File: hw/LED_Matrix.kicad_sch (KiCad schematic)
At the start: 0 parts

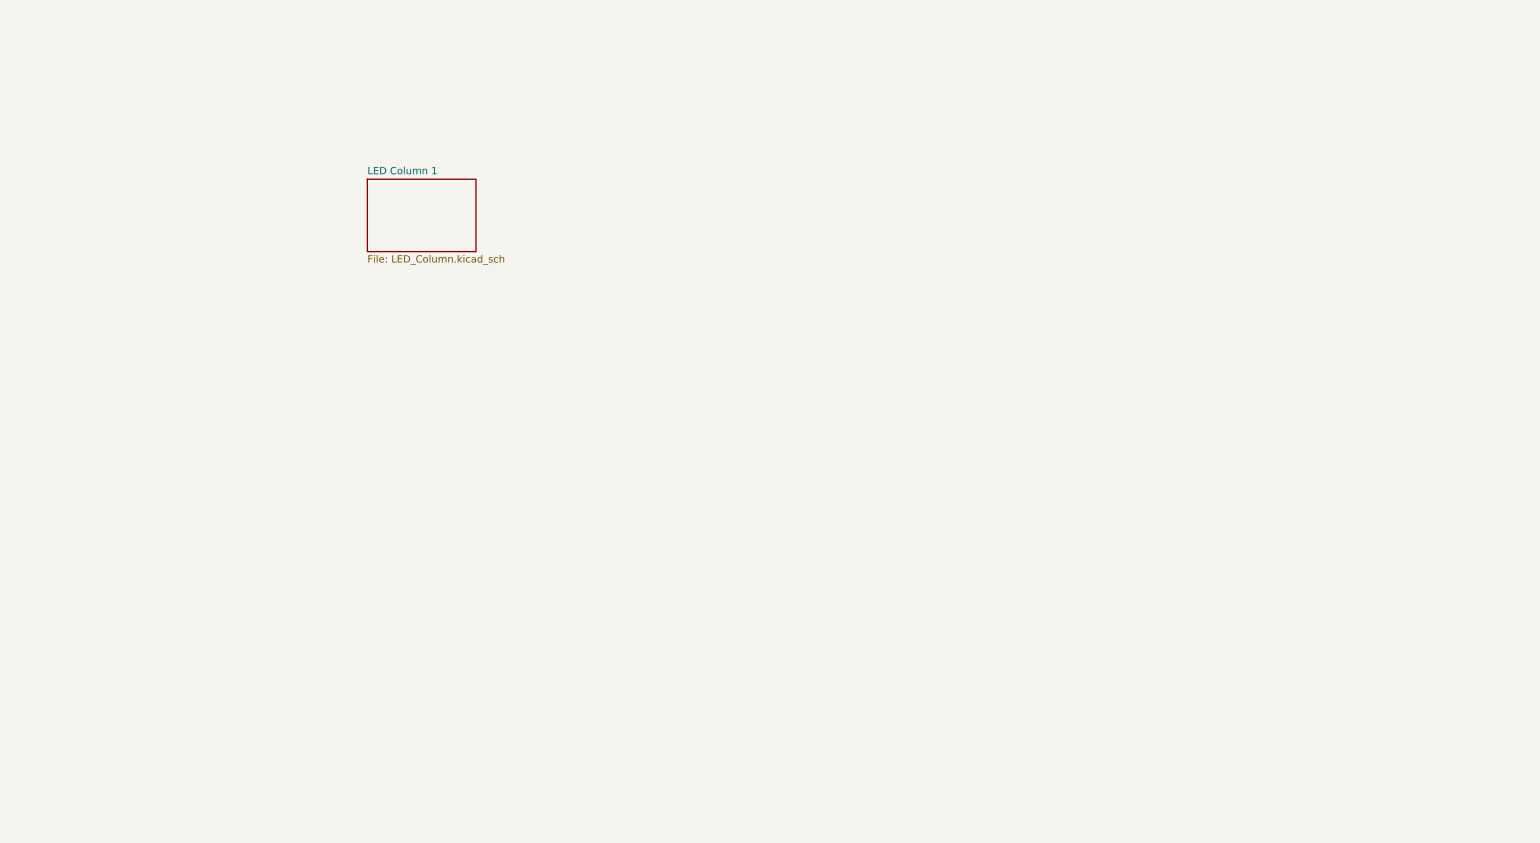
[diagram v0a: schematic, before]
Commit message: added LED Matrix sch
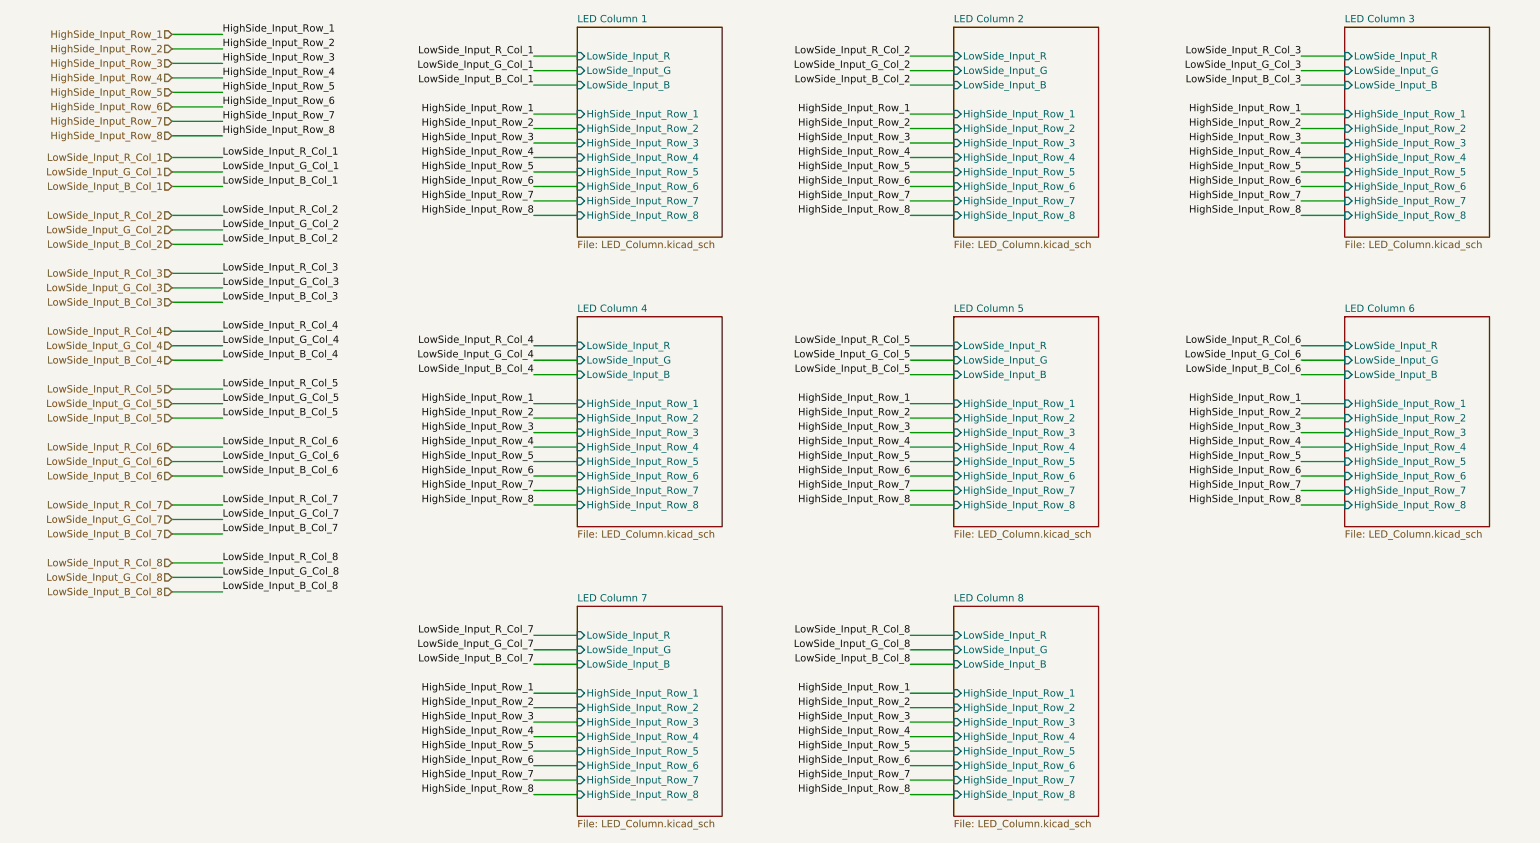
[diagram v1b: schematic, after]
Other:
- added sheet LED Column 2 (LED_Column.kicad_sch)
- added sheet LED Column 3 (LED_Column.kicad_sch)
- added sheet LED Column 4 (LED_Column.kicad_sch)
- added sheet LED Column 5 (LED_Column.kicad_sch)
- added sheet LED Column 6 (LED_Column.kicad_sch)
- added sheet LED Column 7 (LED_Column.kicad_sch)
- added sheet LED Column 8 (LED_Column.kicad_sch)
- sheet LED Column 1 ports: added HighSide_Input_Row_1, HighSide_Input_Row_2, HighSide_Input_Row_3, HighSide_Input_Row_4, HighSide_Input_Row_5, HighSide_Input_Row_6, HighSide_Input_Row_7, HighSide_Input_Row_8, LowSide_Input_B, LowSide_Input_G, LowSide_Input_R; removed none

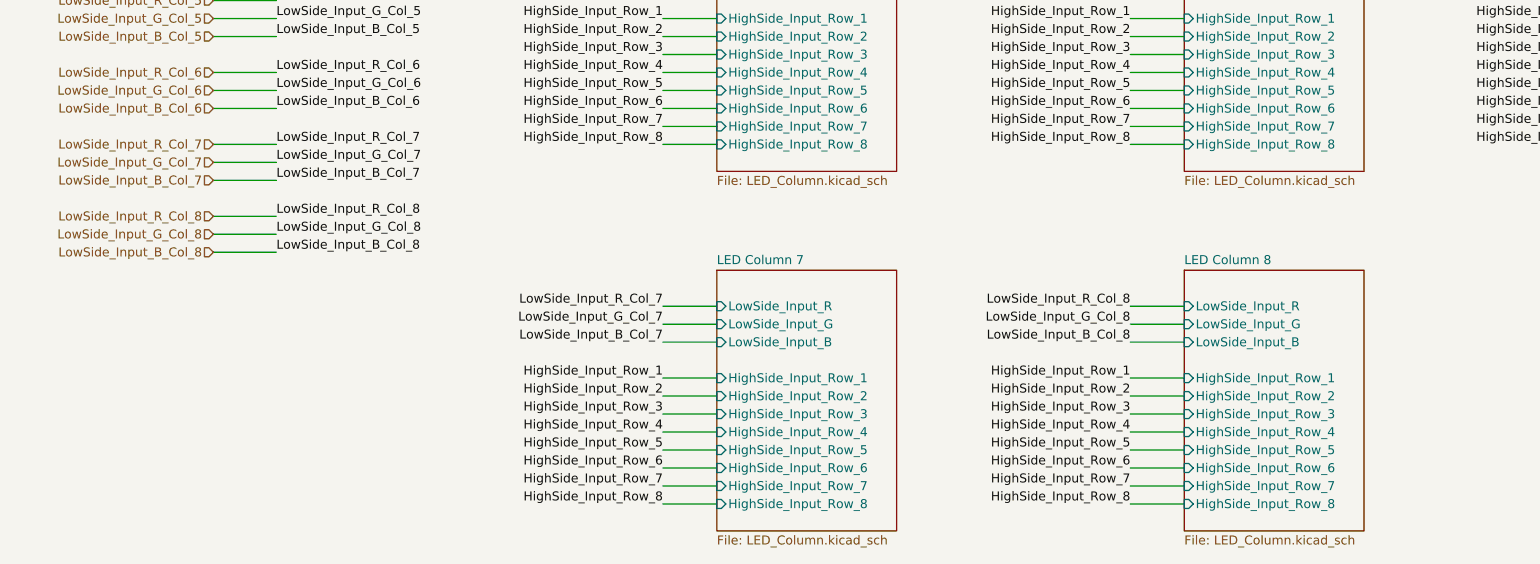
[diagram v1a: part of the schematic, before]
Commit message: updated pin connections
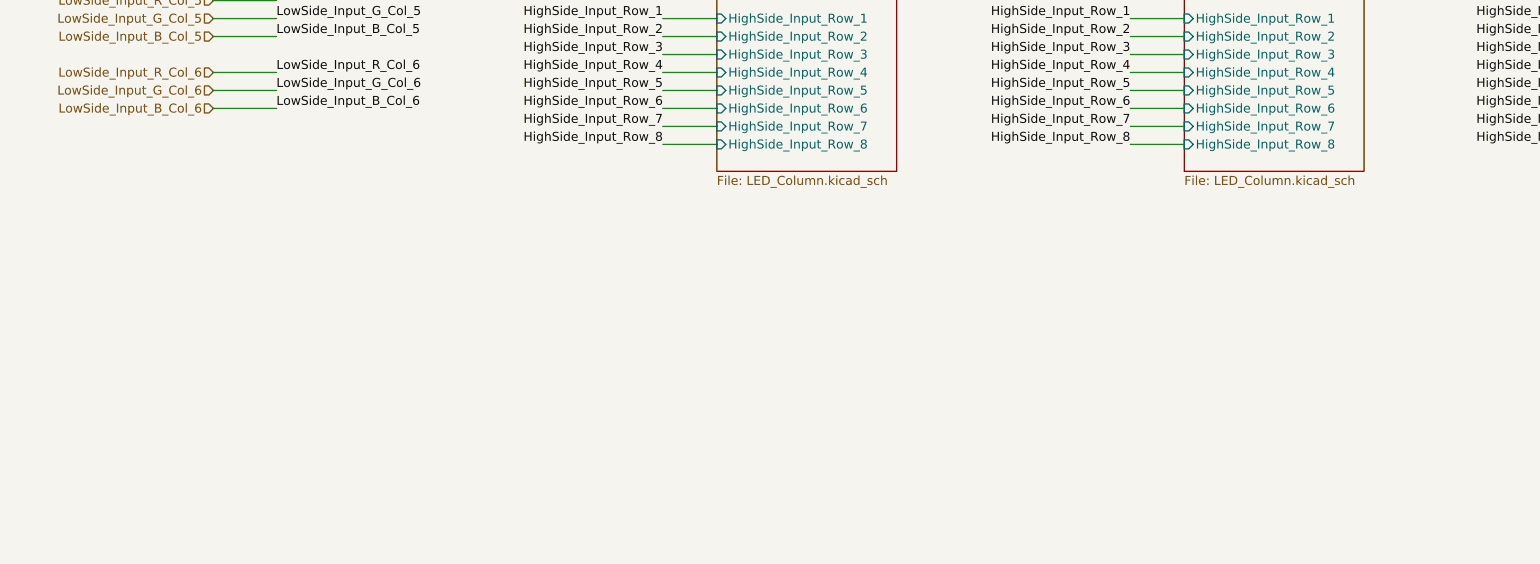
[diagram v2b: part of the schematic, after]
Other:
- removed sheet LED Column 7
- removed sheet LED Column 8
